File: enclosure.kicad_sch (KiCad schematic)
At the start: 16 parts, among them J101 Conn_01x06_Socket

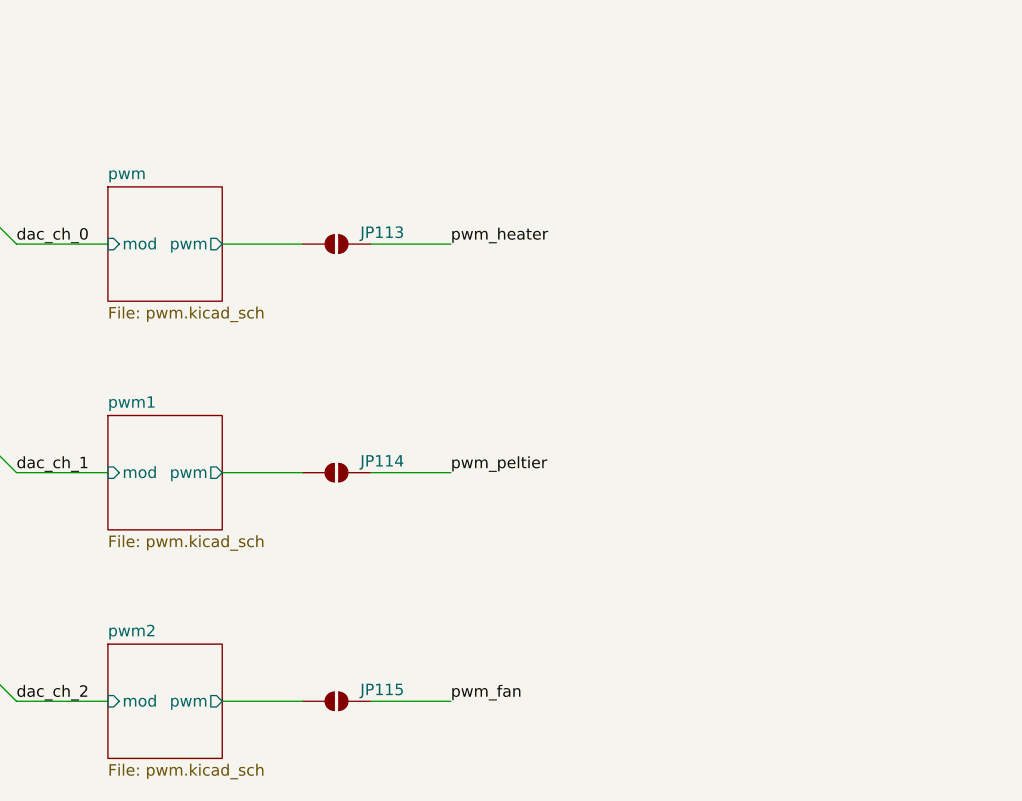
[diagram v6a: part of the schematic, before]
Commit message: add enclosure full-bridge sub circuit
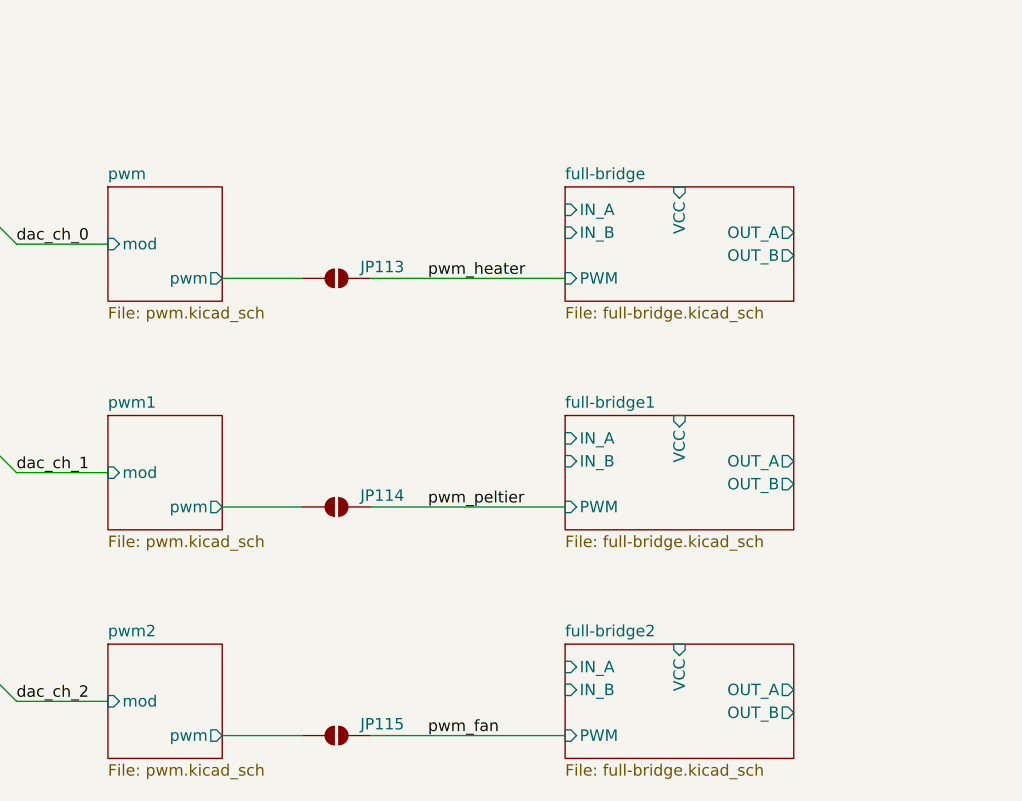
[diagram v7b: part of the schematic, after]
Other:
- added sheet full-bridge (full-bridge.kicad_sch)
- added sheet full-bridge1 (full-bridge.kicad_sch)
- added sheet full-bridge2 (full-bridge.kicad_sch)
- moved on the sheet: JP113, JP114, JP115

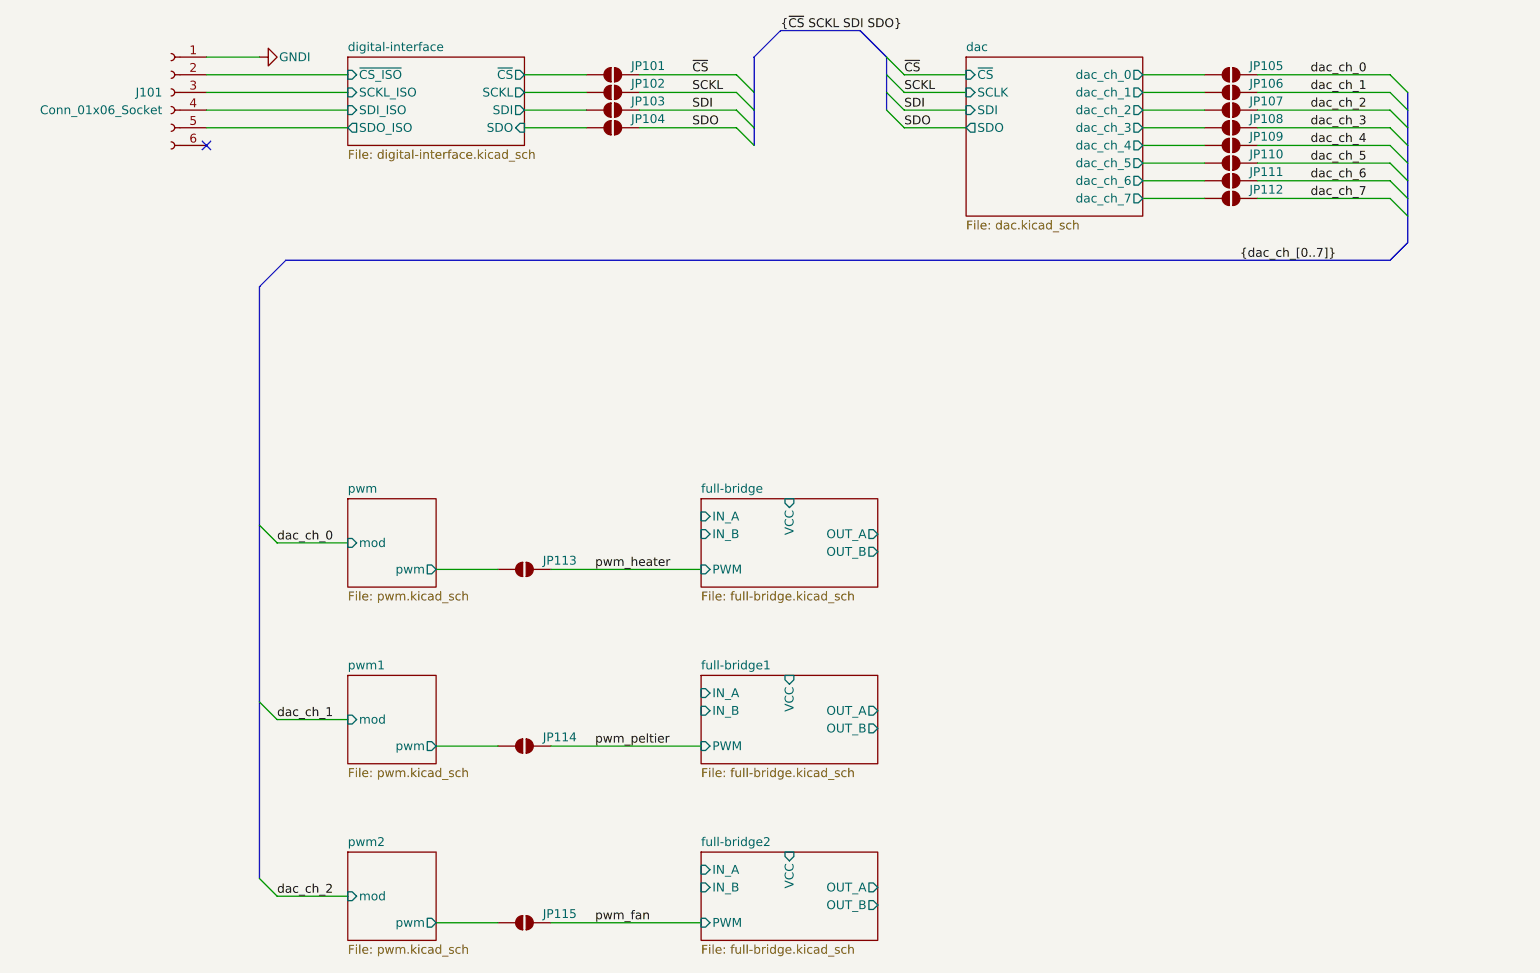
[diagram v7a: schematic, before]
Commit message: add enclosure power sub circuit
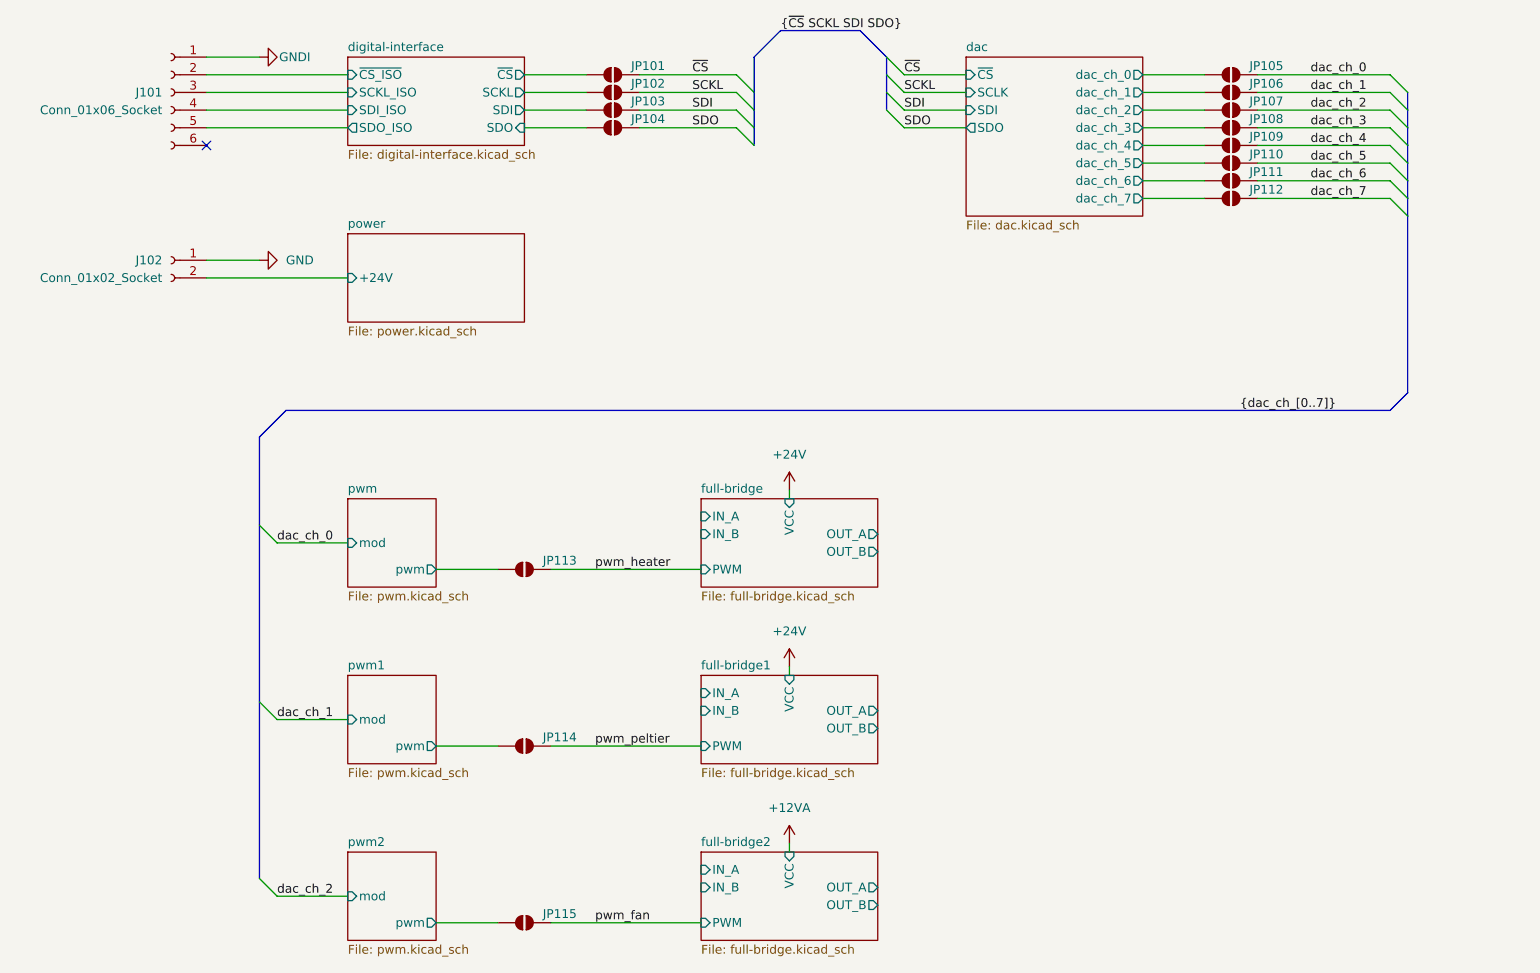
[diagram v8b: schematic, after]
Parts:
- added J102: Conn_01x02_Socket, pss:PhoenixContact_TDPT_2,5_2-SP-5,08_1x02_P5.08mm_Horizontal, symbol enclosure:Conn_01x02_Socket
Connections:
- new net GND: J102.1 (Pin_1)
- new net power/+24V: J102.2 (Pin_2)
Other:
- added sheet power (power.kicad_sch)
